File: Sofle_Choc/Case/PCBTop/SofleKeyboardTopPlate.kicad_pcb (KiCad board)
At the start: 2 copper layers, 143.4 x 111.8 mm, 34 parts, among them SW2 KEY_SWITCH

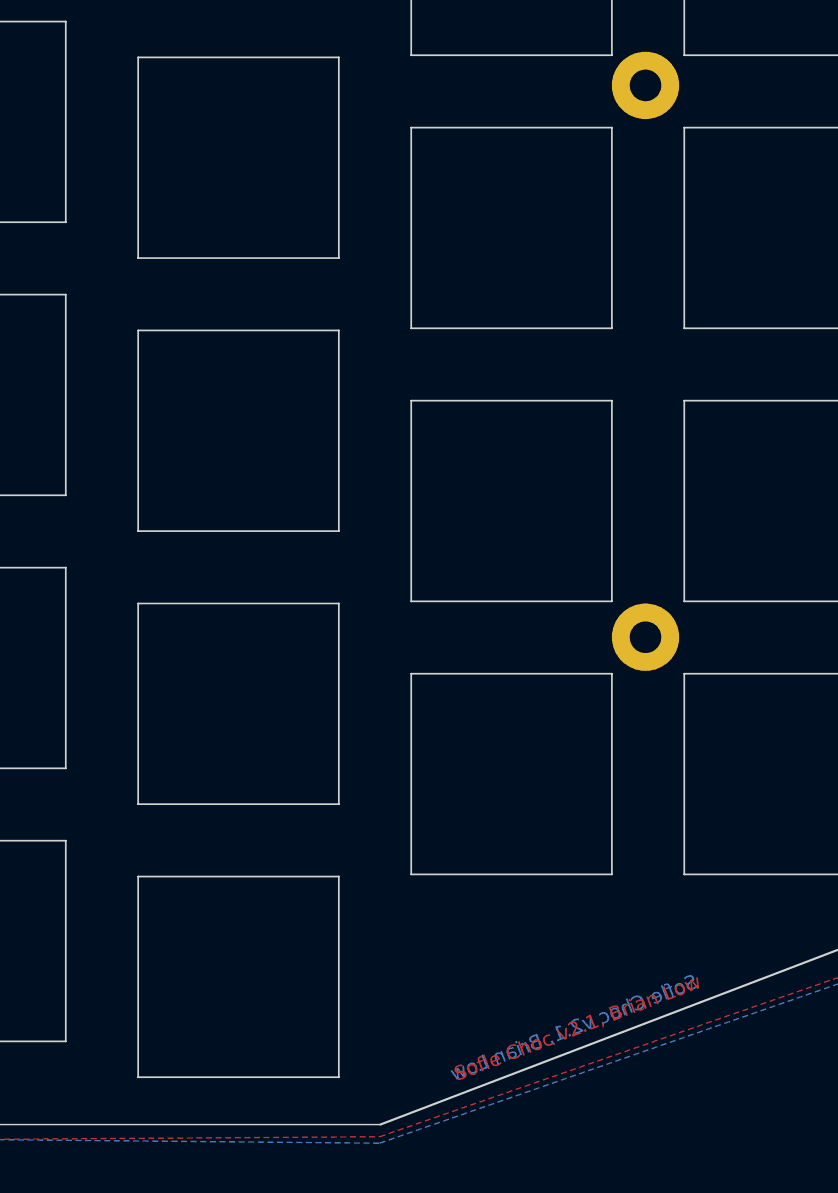
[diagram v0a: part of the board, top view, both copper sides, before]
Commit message: Move top plate version number to less visible location
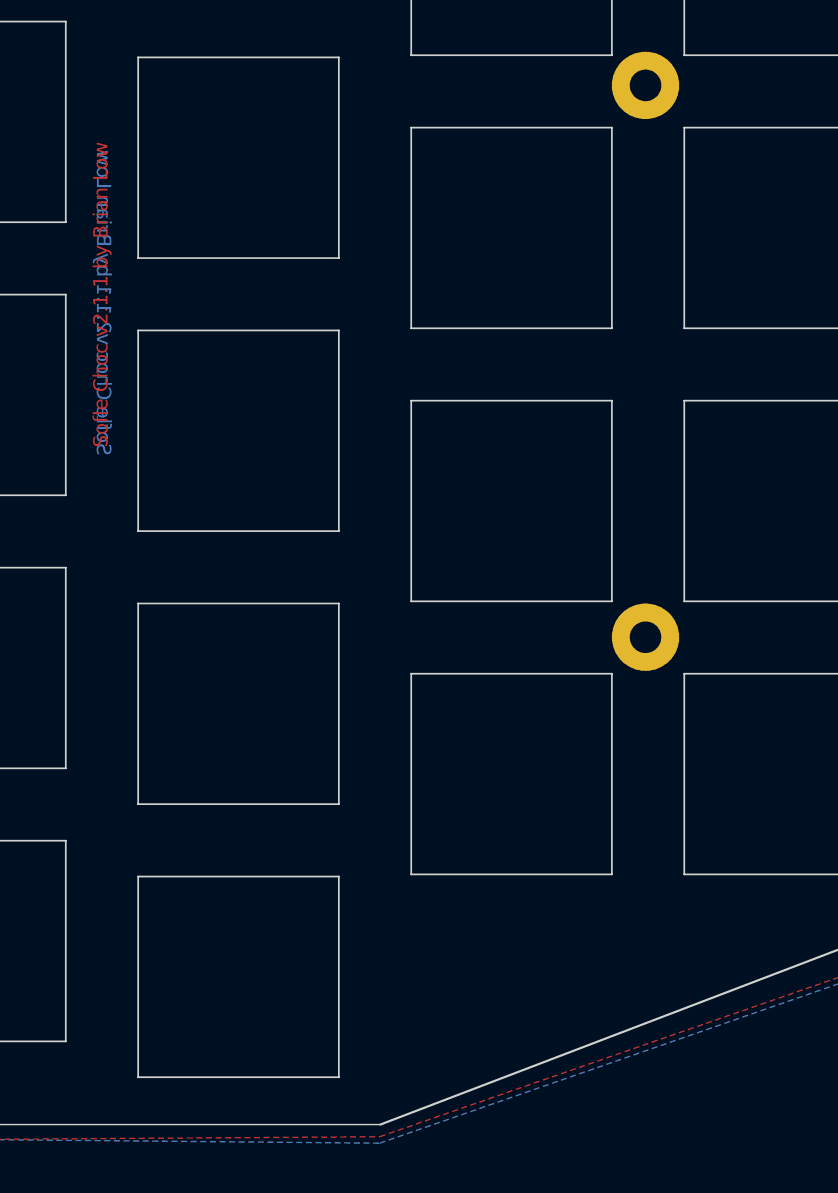
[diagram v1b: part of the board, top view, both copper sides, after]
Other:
- board text added: "Sofle Choc v2.1.1 by Brian Low"
- board text removed: "Sofle Choc v2.1, Brian Low"
